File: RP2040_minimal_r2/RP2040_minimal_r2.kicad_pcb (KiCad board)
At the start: 2 copper layers, 46 x 34 mm, 44 parts, among them J1 SPI0.6, J10 B22, J11 B23, J12 Breakout, J2 SPI0.8, J3 SPI1.13, J4 I2C0, J5 USB, J6 B18, J7 B19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

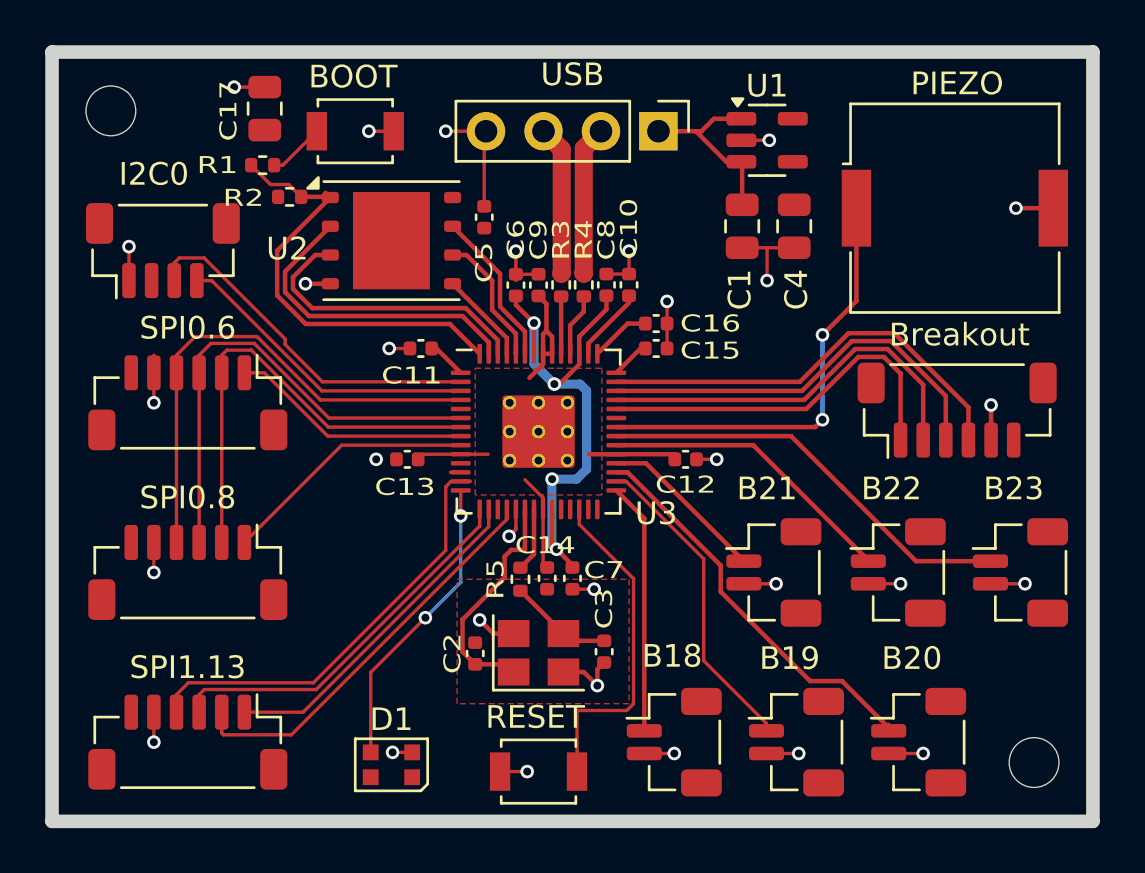
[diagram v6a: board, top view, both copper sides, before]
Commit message: Fix incorrect pins used for SPI0. Changed button pins to GPIO 16-21 for slightly cleaner layout. Moved USB header closer to board edge, to allow JST-XH connector to be attached the other way around. Other minor tweaks to top side layout.
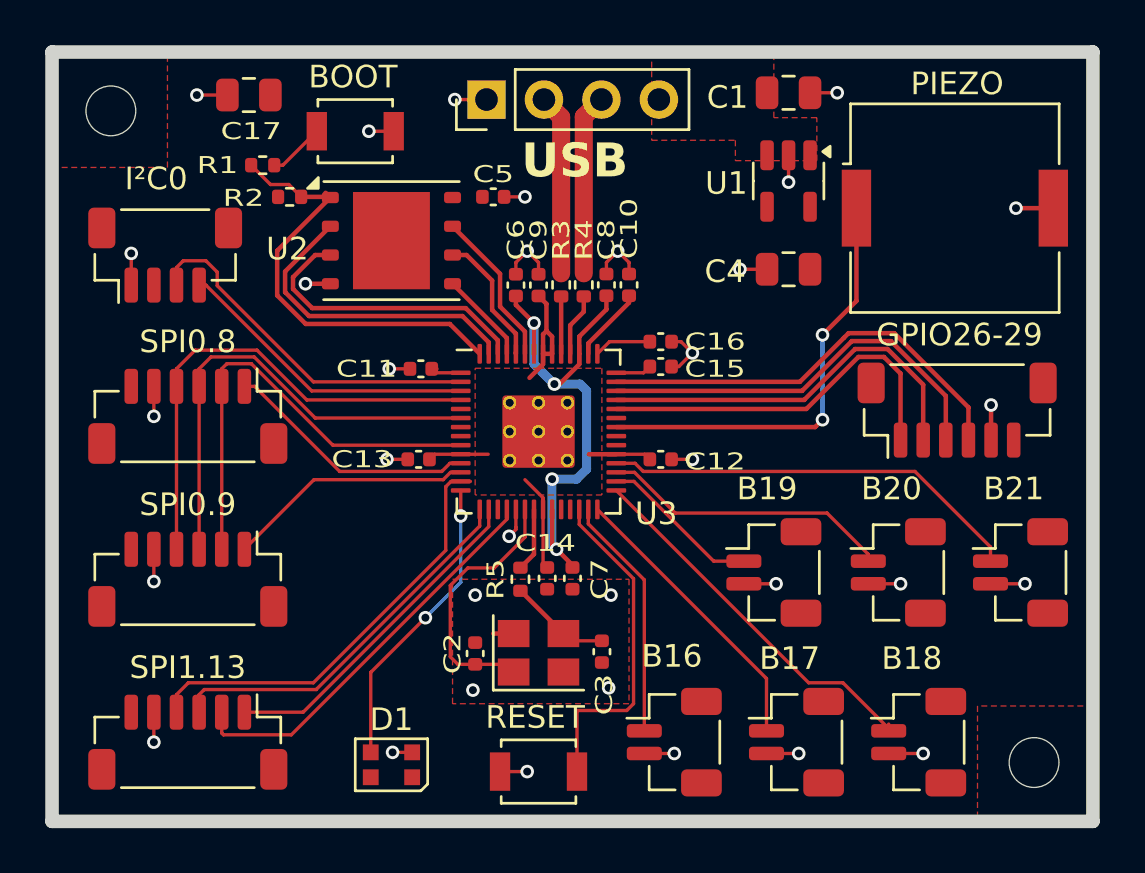
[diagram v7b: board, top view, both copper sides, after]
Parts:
- J1: value SPI0.6 -> SPI0.8
- J10: value B22 -> B20
- J11: value B23 -> B21
- J12: value Breakout -> GPIO26-29
- J2: value SPI0.8 -> SPI0.9
- J4: value I2C0 -> I²C0
- J6: value B18 -> B16
- J7: value B19 -> B17
- J8: value B20 -> B18
- J9: value B21 -> B19
- moved J5 7.73 mm to (96.2, 72.1), turned to 90 degrees
- moved C1 6.25 mm to (109.5, 71.8), turned to 0 degrees
- moved U1 2.04 mm to (109.5, 75.7), turned to -90 degrees
- moved C4 1.92 mm to (109.5, 79.6), turned to 180 degrees
- moved C12 1.10 mm to (103.9, 88.0)
- moved C5 0.98 mm to (96.5, 76.4), turned to 0 degrees
- moved C17 0.92 mm to (85.7, 71.9), turned to 180 degrees
- moved C11 0.90 mm to (93.3, 84.0)
- moved C15 0.82 mm to (103.9, 83.9)
- moved C16 0.82 mm to (103.9, 82.8)
- moved J1 0.60 mm to (83.0, 86.1)
- moved C13 0.50 mm to (93.2, 88.0)
- moved J2 0.30 mm to (83.0, 93.3)
- moved J4 0.22 mm to (82.0, 79.0)
- moved C3 0.10 mm to (101.3, 96.5)
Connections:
- J1 pad 1: NCS06 -> NCS08
- J10 pad 1: GPIO22 -> GPIO20
- J11 pad 1: GPIO23 -> GPIO21
- J2 pad 1: NCS07 -> NCS09
- J5 pad 1: VBUS -> GND
- J5 pad 2: /USB_D- -> /USB_D+
- J5 pad 3: /USB_D+ -> /USB_D-
- J5 pad 4: GND -> VBUS
- J6 pad 1: GPIO18 -> GPIO16
- J7 pad 1: GPIO19 -> GPIO17
- J8 pad 1: GPIO20 -> GPIO18
- J9 pad 1: GPIO21 -> GPIO19
- U3 pad 11: unconnected-(U3-GPIO8-Pad11) -> NCS08
- U3 pad 12: unconnected-(U3-GPIO9-Pad12) -> NCS09
- U3 pad 27: unconnected-(U3-GPIO16-Pad27) -> GPIO16
- U3 pad 28: unconnected-(U3-GPIO17-Pad28) -> GPIO17
- U3 pad 34: GPIO22 -> /GPIO22
- U3 pad 35: GPIO23 -> /GPIO23
- U3 pad 7: MOSI -> unconnected-(U3-GPIO5-Pad7)
- U3 pad 8: NCS06 -> unconnected-(U3-GPIO6-Pad8)
- U3 pad 9: NCS07 -> MOSI
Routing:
- net GPIO23: track 19.0 -> 0.00 mm
- net GPIO22: track 13.3 -> 0.00 mm
- net GPIO17: track 0.00 -> 12.9 mm
- net NCS07: track 11.3 -> 0.00 mm
- net NCS08: track 0.00 -> 11.3 mm
- net GPIO21: track 7.43 -> 18.7 mm
- net NCS09: track 0.00 -> 11.0 mm
- net GPIO16: track 0.00 -> 10.8 mm
- net NCS06: track 10.7 -> 0.00 mm
- net VBUS: track 8.38 -> 0.00 mm
- net GND: track 49.2 -> 41.3 mm, vias 30 -> 33
- net GPIO19: track 14.0 -> 7.10 mm
- net GPIO18: track 11.1 -> 16.9 mm
- net GPIO20: track 17.8 -> 13.0 mm
- net +3V3: track 26.3 -> 24.4 mm
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- added copper zone on F.Cu, net VBUS
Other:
- board text added: "5V"
- board text added: "D+"
- board text added: "D-"
- board text added: "GND"
- board text added: "github.com/monroewilliams/rp2040_mwtrackball"
- board text removed: "https://github.com/monroewilliams/rp2040_mwtrackball"

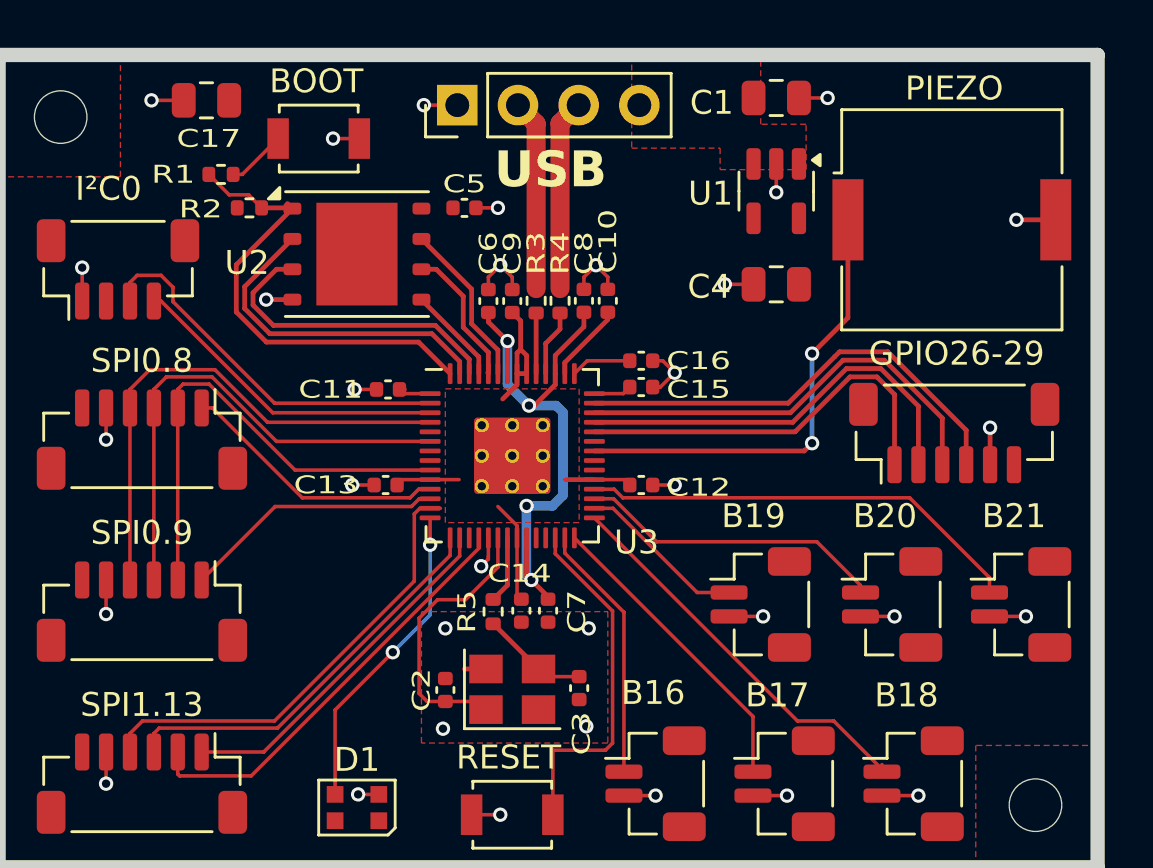
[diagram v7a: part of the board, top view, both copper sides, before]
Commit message: Update the USB connection to use a proper JST-XH footprint. Add local copies of several footprints that need to be tweaked to match JLCPCB's notion of component orientation/origin.
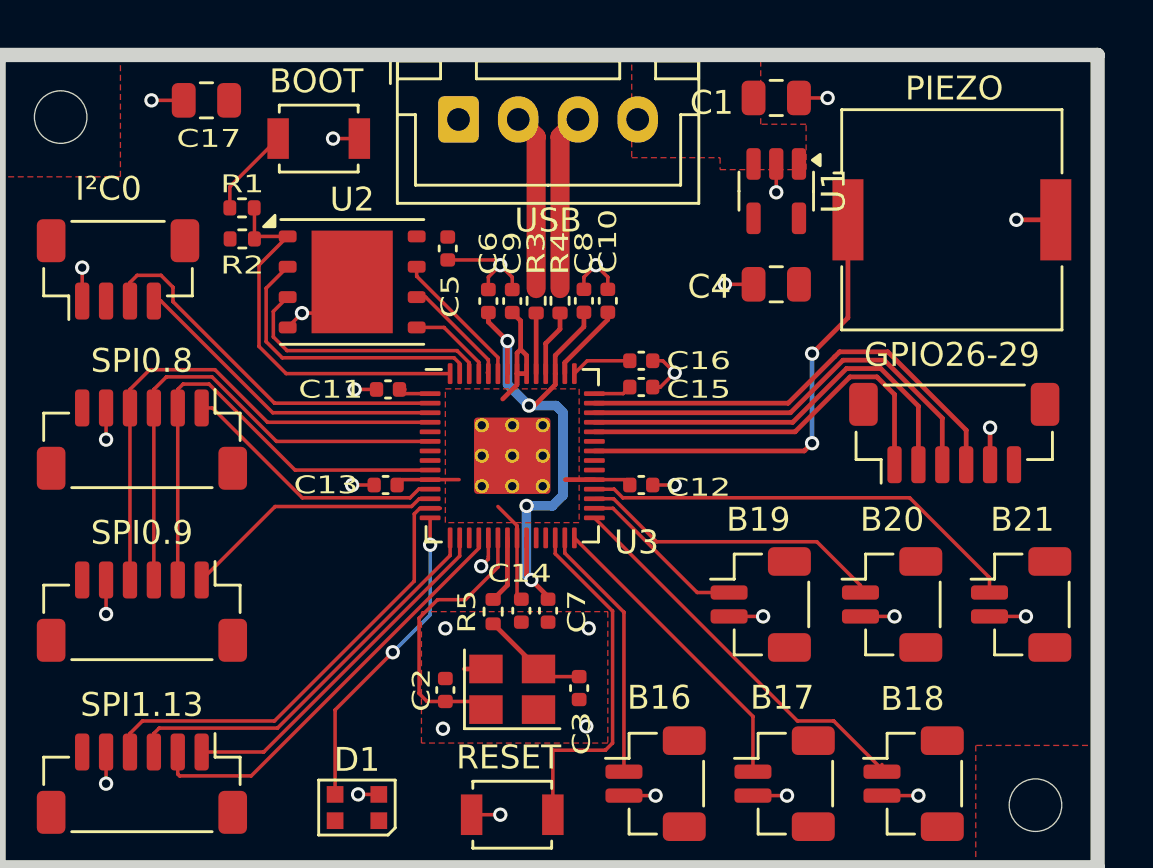
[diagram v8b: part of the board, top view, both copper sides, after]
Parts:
- J1, J12, J2, J3: footprint Connector_JST:JST_SH_BM06B-SRSS-TB_1x06-1MP_P1.00mm_Vertical -> RP2040_minimal:JST_SH_BM06B-SRSS-TB_1x06-1MP_P1.00mm_Vertical
- J10, J11, J6, J7, J8, J9: footprint Connector_JST:JST_SH_BM02B-SRSS-TB_1x02-1MP_P1.00mm_Vertical -> RP2040_minimal:JST_SH_BM02B-SRSS-TB_1x02-1MP_P1.00mm_Vertical
- J5: footprint Connector_PinHeader_2.54mm:PinHeader_1x04_P2.54mm_Vertical -> RP2040_minimal:JST_XH_B4B-XH-A_1x04_P2.50mm_Vertical
- U1: footprint Package_TO_SOT_SMD:SOT-23-5 -> RP2040_minimal:SOT-23-5
- U2: footprint Package_SON:WSON-8-1EP_6x5mm_P1.27mm_EP3.4x4.3mm -> RP2040_minimal:WSON-8-1EP_6x5mm_P1.27mm_EP3.4x4.3mm
- moved J5 3.85 mm to (100.0, 72.7), turned to 180 degrees
- moved C5 1.84 mm to (95.8, 78.1), turned to -90 degrees
- moved R1 1.65 mm to (87.2, 76.4), turned to 180 degrees
- moved R2 1.33 mm to (87.2, 77.7)
- moved U2 1.18 mm to (91.8, 79.5), turned to -90 degrees
- turned J1 to 0 degrees
- turned J10 to 90 degrees
- turned J11 to 90 degrees
- turned J12 to 180 degrees
- turned J2 to 0 degrees
- turned J3 to 0 degrees
- turned J6 to 90 degrees
- turned J7 to 90 degrees
- turned J8 to 90 degrees
- turned J9 to 90 degrees
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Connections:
- U2 pad 9: (no net) -> GND
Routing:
- net /QSPI_SS: track 19.9 -> 16.5 mm
- net GND: track 41.3 -> 43.7 mm, vias 33 -> 31
- net /QSPI_SD2: track 13.2 -> 11.0 mm
- net /QSPI_SD1: track 14.2 -> 12.4 mm
- net /QSPI_SD3: track 7.40 -> 5.88 mm
- net Net-(R1-Pad2): track 2.50 -> 3.74 mm
- net /QSPI_SCLK: track 5.96 -> 4.73 mm
- net /USB_D+: track 8.00 -> 7.42 mm
- net /USB_D-: track 7.99 -> 7.42 mm
